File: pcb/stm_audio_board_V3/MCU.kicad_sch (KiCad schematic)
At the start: 16 parts, among them SW1 SW_SPST, U1 STM32H747IGTx, Y2 X1E0000210132

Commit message: audio_board_v3 added
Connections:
- net +3.3V: no longer U1.113 (VDD), U1.126 (VDD), U1.13 (VDD), U1.136 (VDD), U1.152 (VDD), U1.160 (VDD), U1.176 (VDD), U1.25 (VDD), U1.44 (VDD), U1.48 (VDD), U1.65 (VDD), U1.7 (VDD), U1.71 (VDD), U1.8 (VBAT), U1.84 (VDD), U1.92 (VDD), U1.99 (VDD)
- new net: U1.113 (VDD), U1.126 (VDD), U1.13 (VDD), U1.136 (VDD), U1.152 (VDD), U1.160 (VDD), U1.176 (VDD), U1.25 (VDD), U1.44 (VDD), U1.48 (VDD), U1.65 (VDD), U1.7 (VDD), U1.71 (VDD), U1.8 (VBAT), U1.84 (VDD), U1.92 (VDD), U1.99 (VDD)
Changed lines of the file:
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@@
   (junction (at 204.47 40.64) (diameter 0) (color 0 0 0 0)
   )
-  (junction (at 227.33 40.64) (diameter 0) (color 0 0 0 0)
-  )
   (junction (at 201.93 40.64) (diameter 0) (color 0 0 0 0)
   )
@@
   )
   (wire (pts (xy 326.39 77.47) (xy 326.39 76.2))
-    (stroke (width 0) (type default))
-  )
-  (wire (pts (xy 227.33 39.37) (xy 227.33 40.64))
     (stroke (width 0) (type default))
   )
@@
         )
       )
-    )
-  )
-  (symbol (lib_id "power:+3.3V") (at 227.33 39.37 0) (unit 1)
-    (in_bom yes) (on_board yes) (dnp no) (fields_autoplaced)
-    (property "Reference" "#PWR081" (at 227.33 43.18 0)
-      (effects (font (size 1.27 1.27)) hide)
-    )
-    (property "Value" "+3.3V" (at 227.33 35.56 0)
-      (effects (font (size 1.27 1.27)))
-    )
-    (property "Footprint" "" (at 227.33 39.37 0)
-      (effects (font (size 1.27 1.27)) hide)
-    )
-    (property "Datasheet" "" (at 227.33 39.37 0)
-      (effects (font (size 1.27 1.27)) hide)
-    )
-    (pin "1")
-    (instances
-      (project "stm_audio_board_V2_1"
-        (path "/6997cf63-2615-4e49-9471-e7da1b6bae71/2eb2ee8f-ab98-4666-97f0-bfacb073bc88"
-          (reference "#PWR081") (unit 1)
-        )
-        (path "/6997cf63-2615-4e49-9471-e7da1b6bae71/51aec99e-3301-49b6-8e7f-31ba63a05d64"
-          (reference "#PWR057") (unit 1)
-        )
-      )

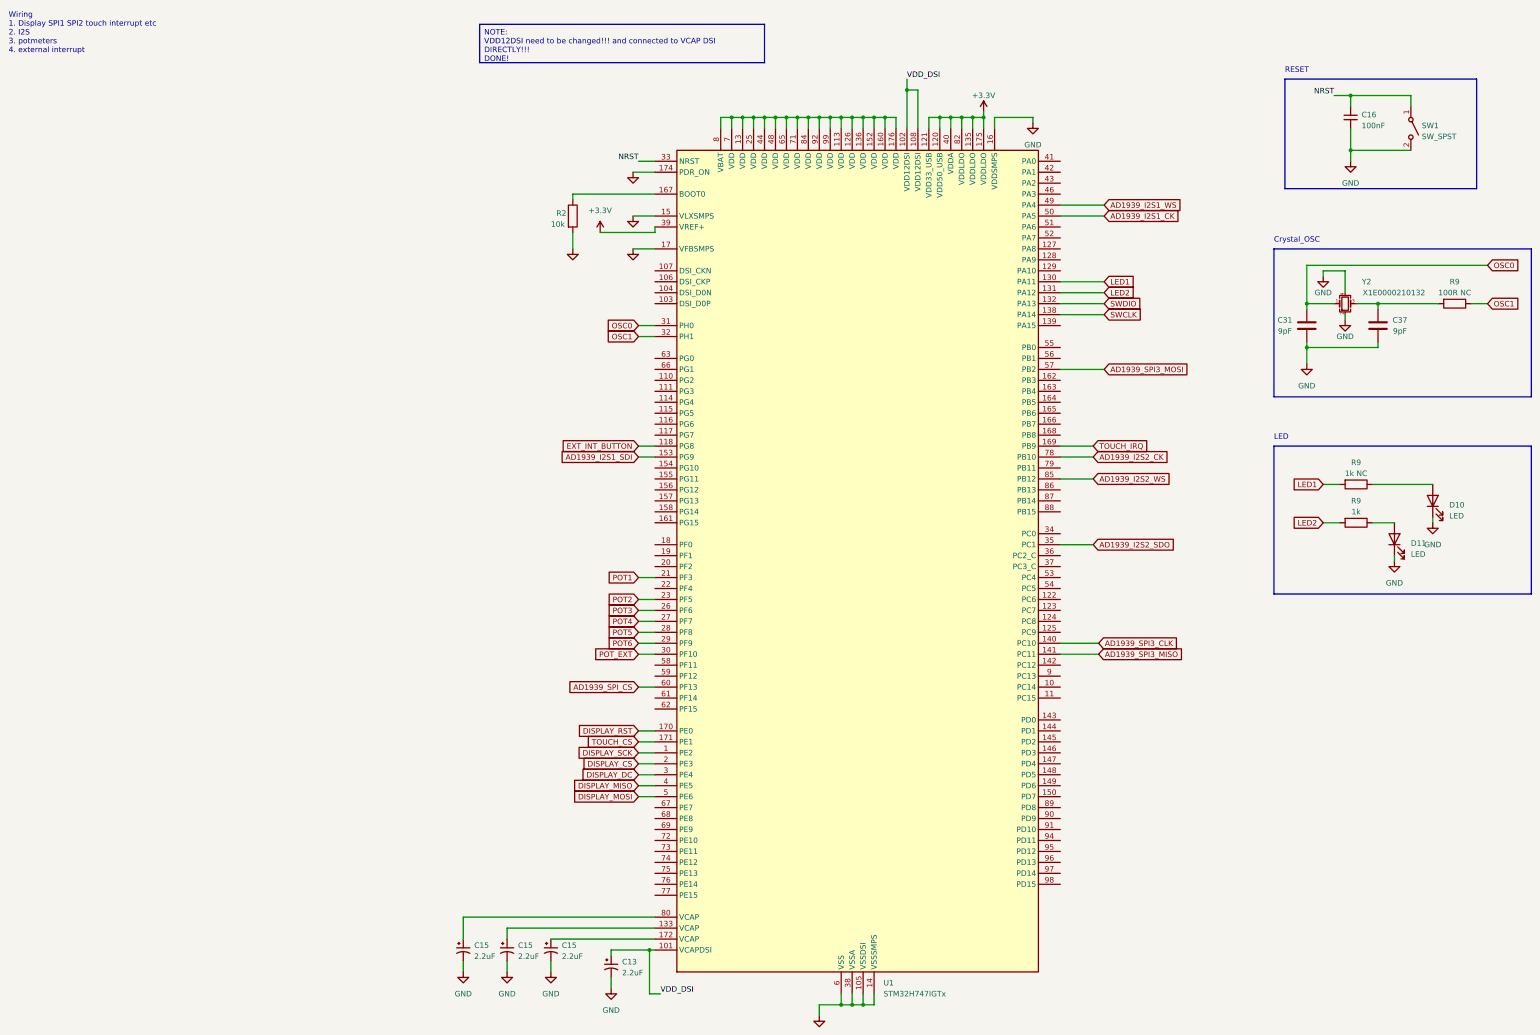
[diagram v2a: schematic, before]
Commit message: stm32h723 project for pinout added
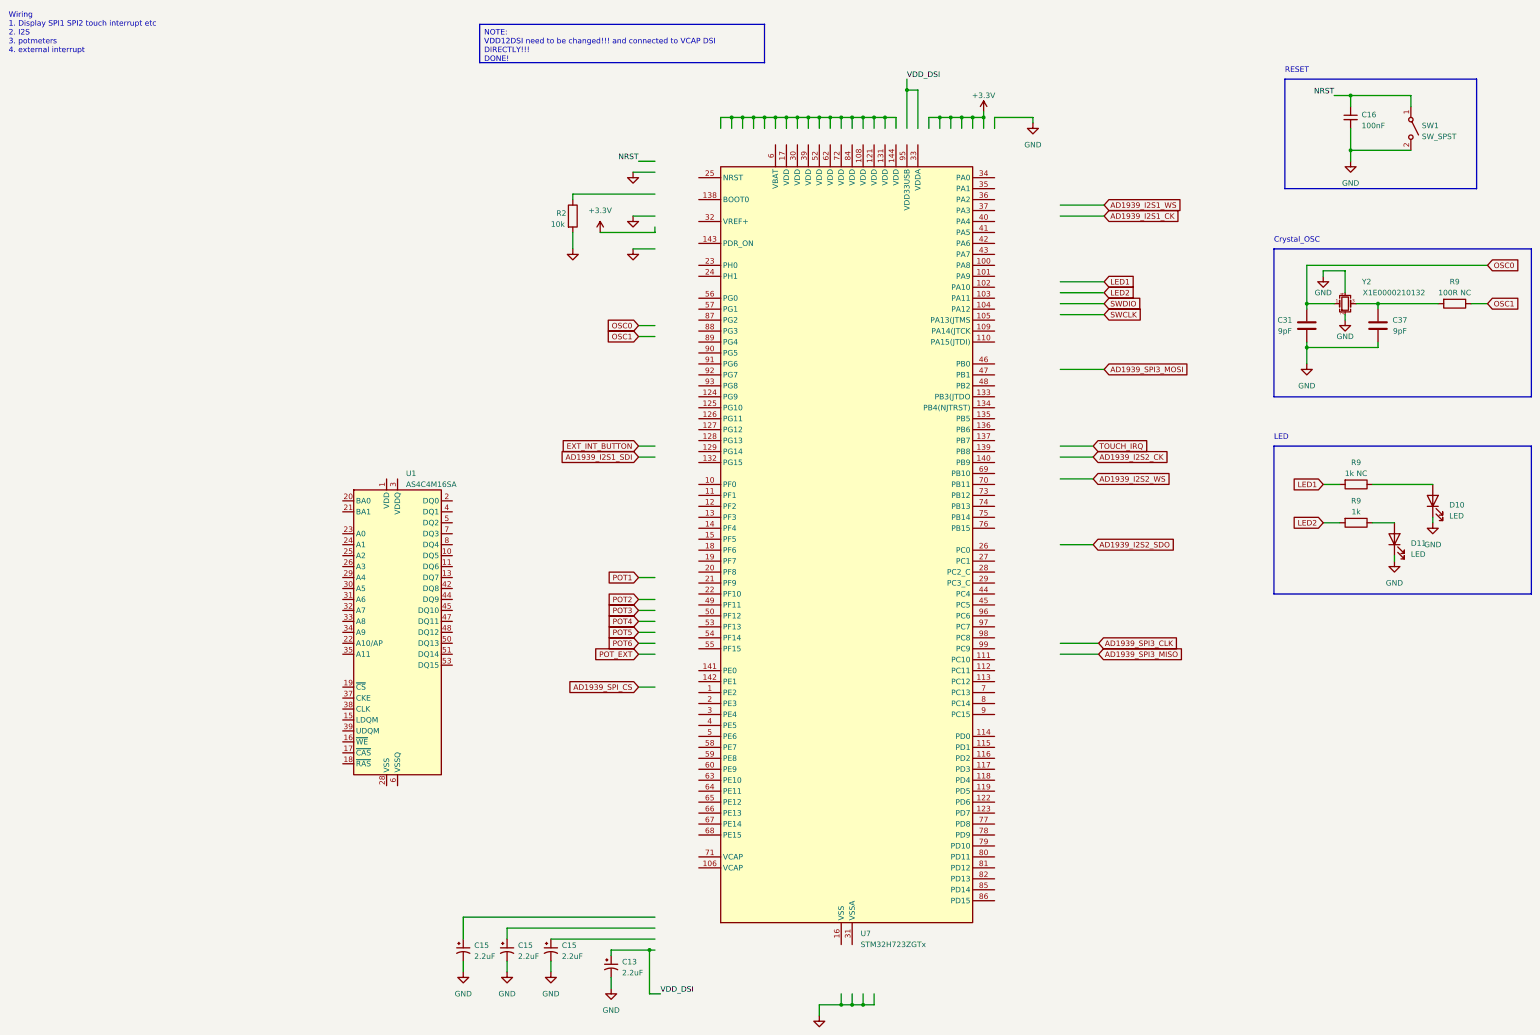
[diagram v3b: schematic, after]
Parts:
- removed U1: STM32H747IGTx, Package_QFP:LQFP-176_24x24mm_P0.5mm, symbol MCU_ST_STM32H7:STM32H747IGTx
- added U1: AS4C4M16SA, Package_SO:TSOP-II-54_22.2x10.16mm_P0.8mm, symbol Memory_RAM:AS4C4M16SA
- added U7: STM32H723ZGTx, Package_QFP:LQFP-144_20x20mm_P0.5mm, symbol MCU_ST_STM32H7:STM32H723ZGTx
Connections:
- new net: U7.107 (VSS), U7.120 (VSS), U7.130 (VSS), U7.16 (VSS), U7.38 (VSS), U7.51 (VSS), U7.61 (VSS), U7.83 (VSS), U7.94 (VSS)
- new net: U1.1 (VDD), U1.14 (VDD), U1.27 (VDD)
- new net: U1.12 (VSSQ), U1.46 (VSSQ), U1.52 (VSSQ), U1.6 (VSSQ)
- new net: U1.28 (VSS), U1.41 (VSS), U1.54 (VSS)
- new net: U1.3 (VDDQ), U1.43 (VDDQ), U1.49 (VDDQ), U1.9 (VDDQ)

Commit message: v3 pcb updated pinout generated form cubeide
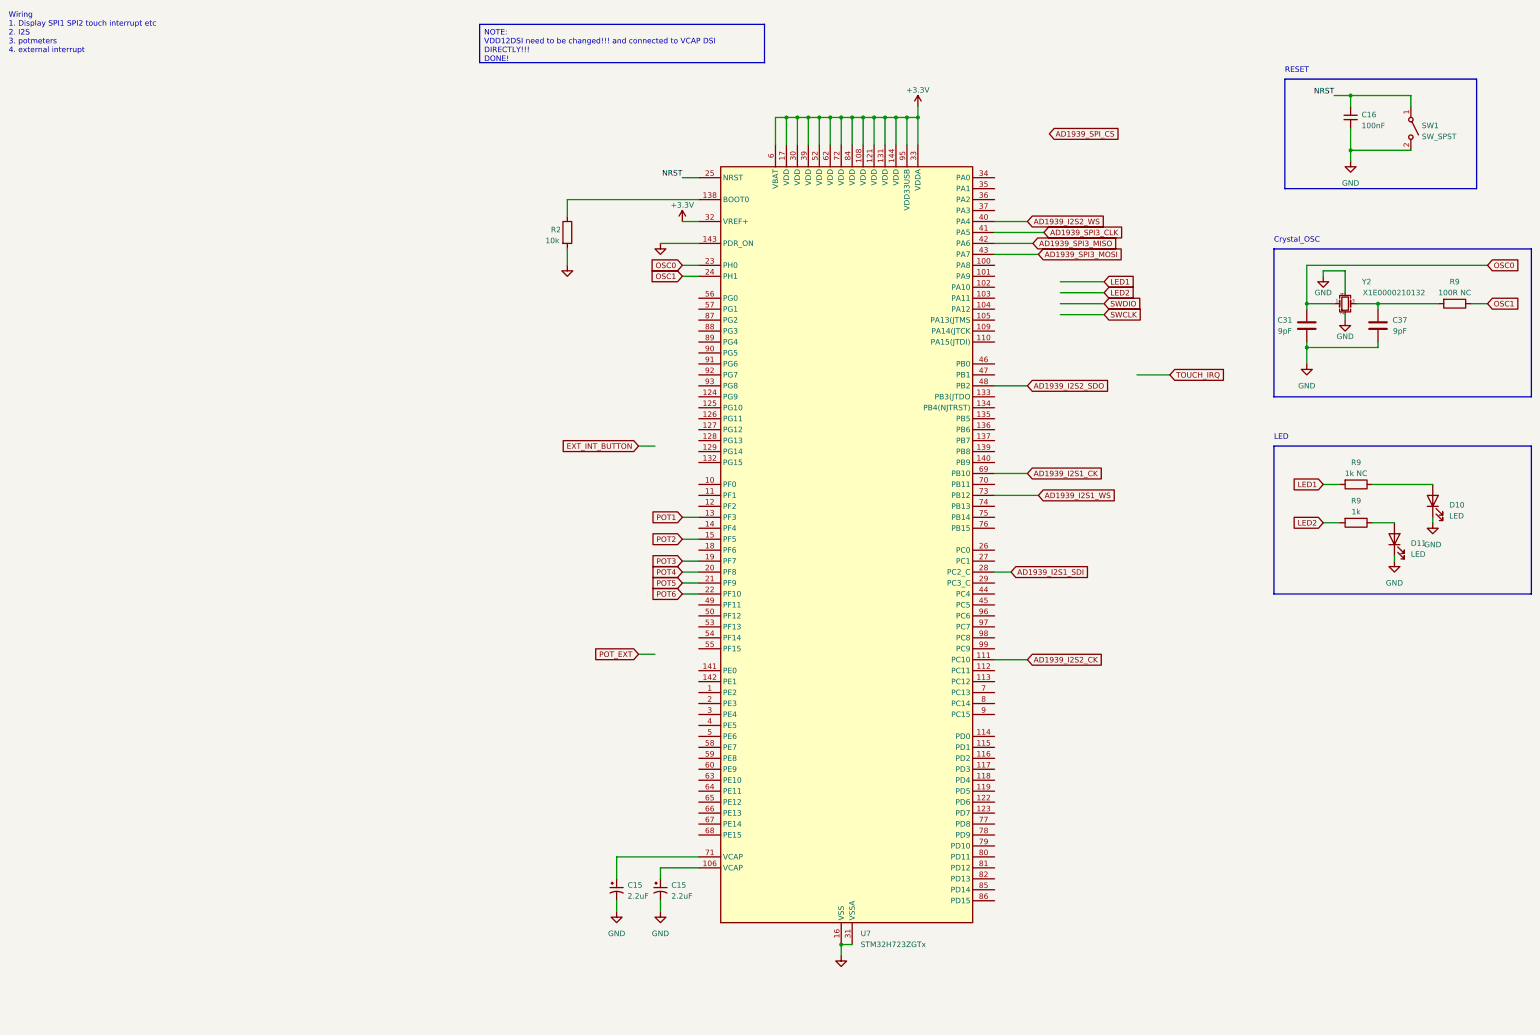
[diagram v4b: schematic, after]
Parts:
- removed C13, C15: 2.2uF, Capacitor_SMD:C_0805_2012Metric_Pad1.18x1.45mm_HandSolder, symbol Device:C_Polarized_Small_US
- removed U1: AS4C4M16SA, Package_SO:TSOP-II-54_22.2x10.16mm_P0.8mm, symbol Memory_RAM:AS4C4M16SA
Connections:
- net +3.3V: now also U7.108 (VDD), U7.121 (VDD), U7.131 (VDD), U7.144 (VDD), U7.17 (VDD), U7.30 (VDD), U7.32 (VREF+), U7.33 (VDDA), U7.39 (VDD), U7.52 (VDD), U7.6 (VBAT), U7.62 (VDD), U7.72 (VDD), U7.84 (VDD), U7.95 (VDD33USB)
- net AD1939_I2S1_CK: now also U7.69 (PB10)
- net AD1939_I2S1_SDI: now also U7.28 (PC2_C)
- net AD1939_I2S1_WS: now also U7.73 (PB12)
- net AD1939_I2S2_CK: now also U7.111 (PC10)
- net AD1939_I2S2_SDO: now also U7.48 (PB2)
- net AD1939_I2S2_WS: now also U7.40 (PA4)
- net AD1939_SPI3_CLK: now also U7.41 (PA5)
- net AD1939_SPI3_MISO: now also U7.42 (PA6)
- net AD1939_SPI3_MOSI: now also U7.43 (PA7)
- net GND: now also U7.107 (VSS), U7.120 (VSS), U7.130 (VSS), U7.143 (PDR_ON), U7.16 (VSS), U7.31 (VSSA), U7.38 (VSS), U7.51 (VSS), U7.61 (VSS), U7.83 (VSS), U7.94 (VSS)
- net NRST: now also U7.25 (NRST)
- net OSC0: now also U7.23 (PH0)
- net OSC1: now also U7.24 (PH1)
- net POT1: now also U7.13 (PF3)
- net POT2: now also U7.15 (PF5)
- net POT3: now also U7.19 (PF7)
- net POT4: now also U7.20 (PF8)
- net POT5: now also U7.21 (PF9)
- net POT6: now also U7.22 (PF10)
- net at C15.1: now also U7.71 (VCAP)
- net at U7.106 (VCAP): now also C15.1
- net at U7.138 (BOOT0): now also R2.1
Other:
- moved on the sheet: C15, R2
